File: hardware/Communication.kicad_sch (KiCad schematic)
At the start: 18 parts, among them U1 USBLC6-2SC6, U3 MCP2542FDxMF, U4 USBLC6-2SC6, U6 MCP2542FDxMF

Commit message: symbol update
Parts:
- U3, U6: value MCP2542FDxMF -> MCP2542FD-E/MF; Manufacturer_Part_Number MCP2542FDT-H/MNY -> MCP2542FD-E/MF; Mouser Part Number 579-MCP2542FDT-H/MNY -> 579-MCP2542FD-E/MF; Mouser Price/Stock https://www.mouser.pl/ProductDetail/Microchip-Technology/MCP2542FDT-H-MNY?qs=qdgZG5p0FZ5ii0%252BaLco0zA%3D%3D -> https://www.mouser.pl/ProductDetail/Microchip-Technology/MCP2542FD-E-MF?qs=l7cgNqFNU1jog4BwTzULBw%3D%3D
- renumbered O2 to O5, R40 to R12, R44 to R13, R67 to R15, R45 to R20

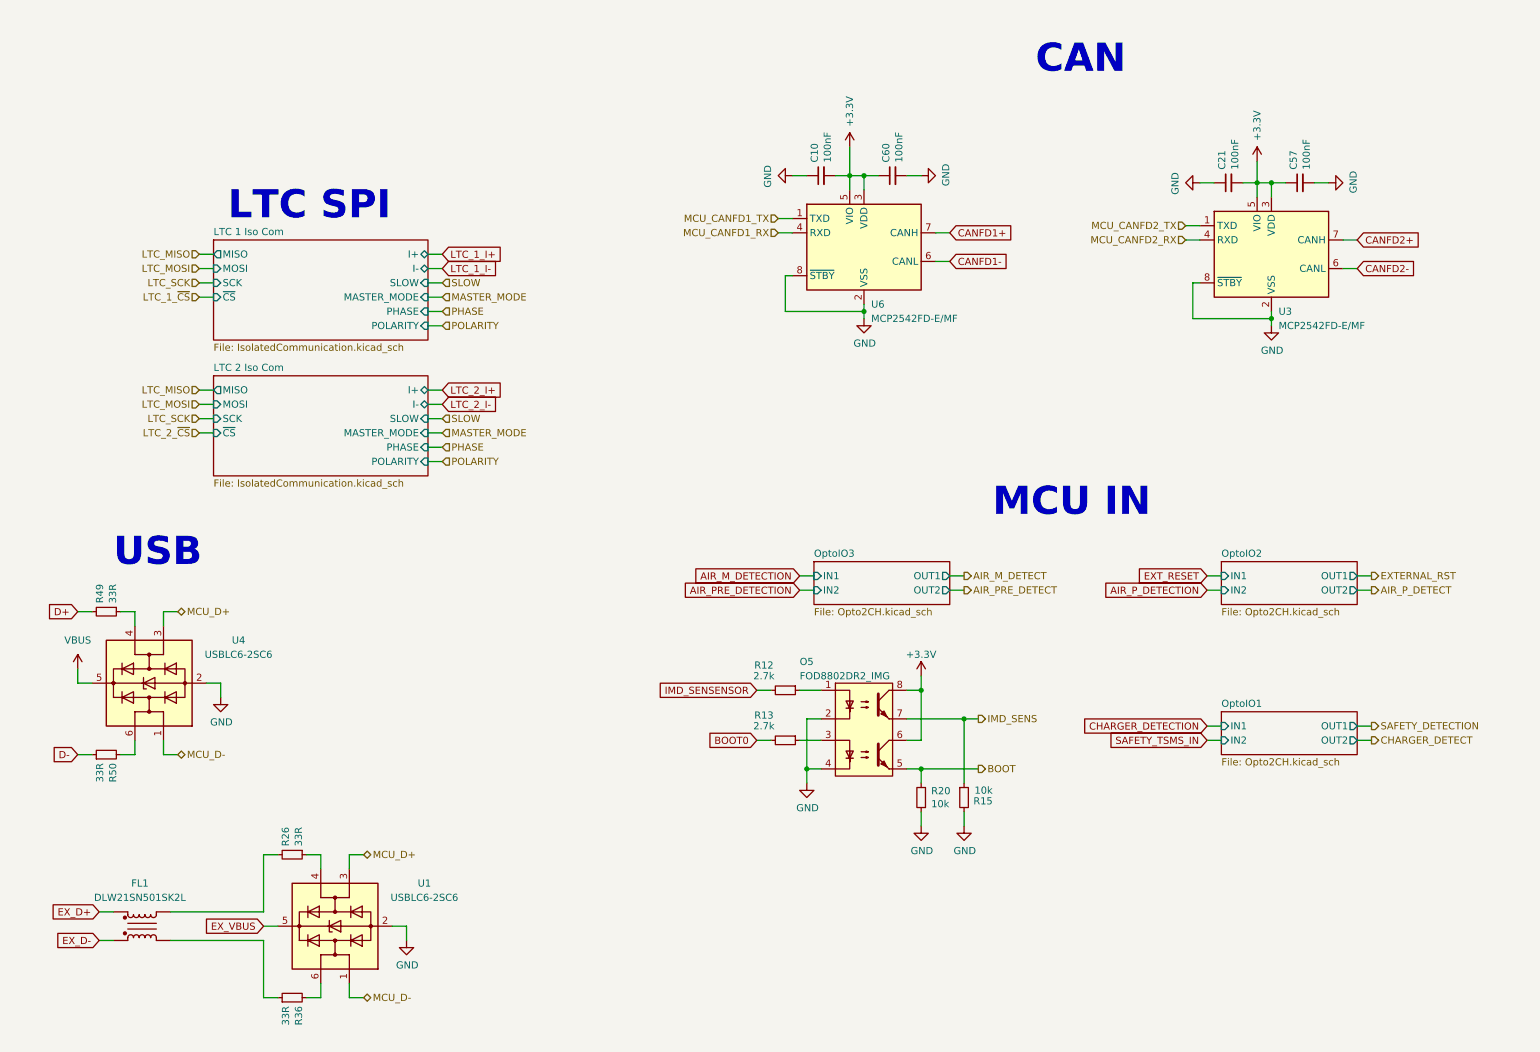
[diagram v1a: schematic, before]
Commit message: schematic clean up
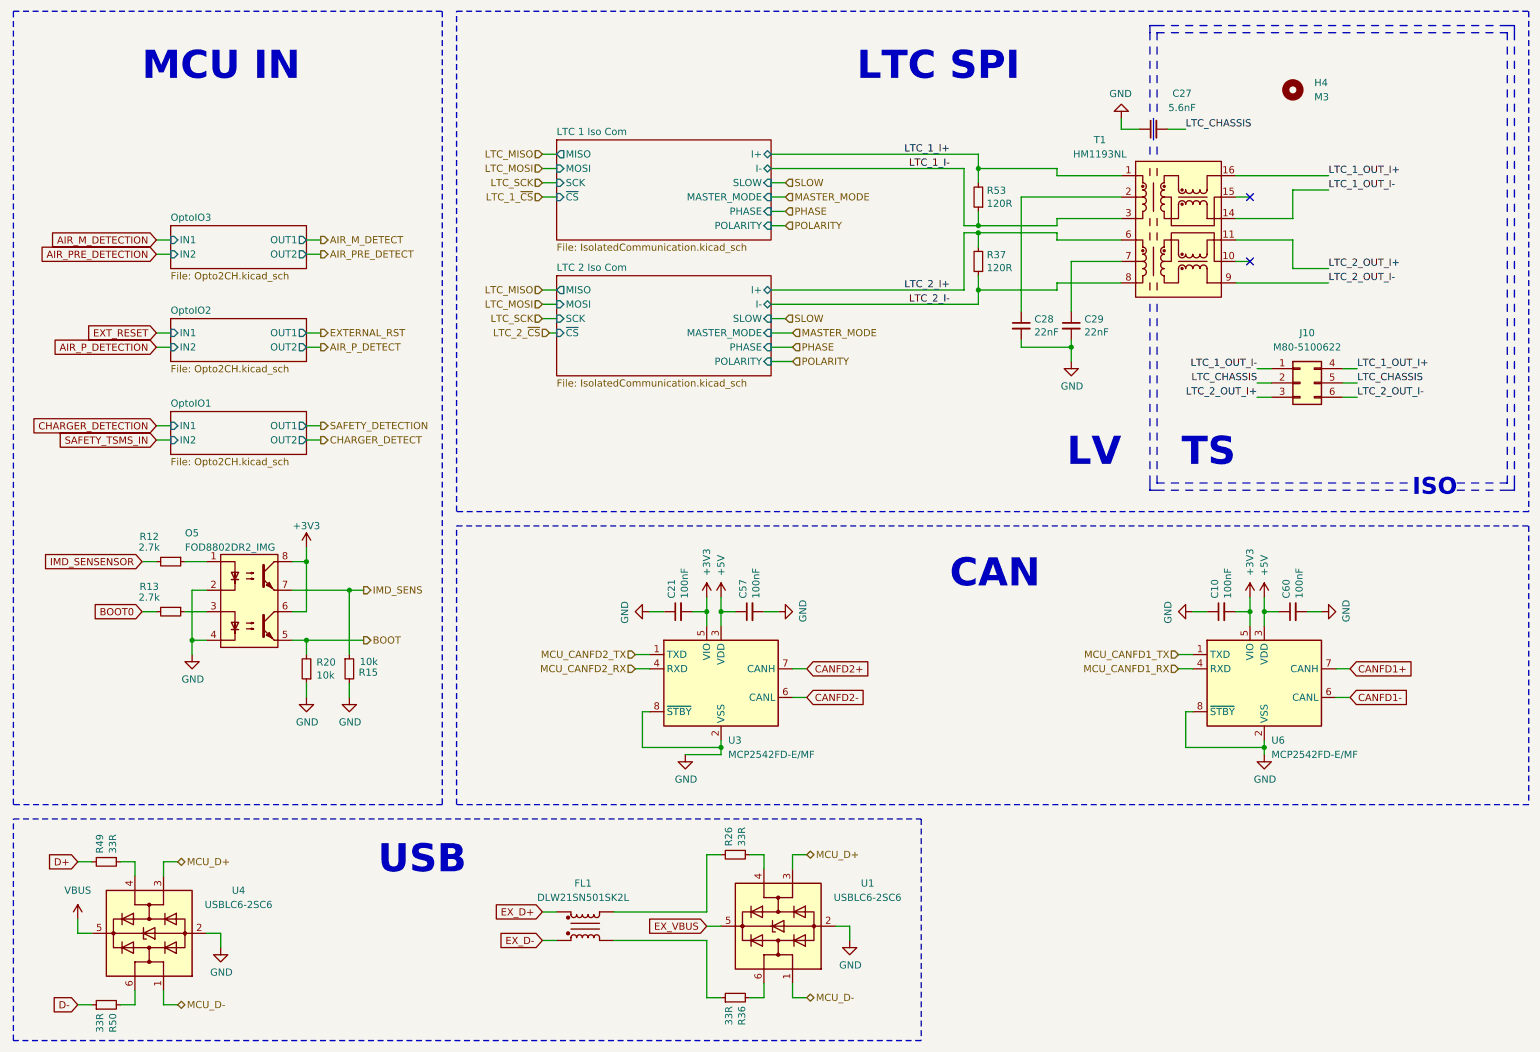
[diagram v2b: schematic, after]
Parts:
- added C27: 5.6nF, Samacsys:C2824, symbol c2824c562jggacauto:C2824C562JGGACAUTO
- added C28, C29: 22nF, Capacitor_SMD:C_0603_1608Metric, symbol Device:C_Small
- added H4: M3, MountingHole:MountingHole_3.2mm_M3, symbol Mechanical:MountingHole
- added J10: M80-5100622, Samacsys:M80-51006YY, symbol Samacsys2:M80-5100622
- added R37, R53: 120R, Resistor_SMD:R_0603_1608Metric, symbol Device:R_Small
- added T1: HM1193NL, Transformer_SMD:Transformer_Pulse_H1100NL, symbol PUTM_EV_BMS_library:HX1188NL
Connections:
- net +3V3: no longer C57.1, C60.1, U3.3 (VDD), U6.3 (VDD)
- net GND: now also C27.1, C28.2, C29.2
- net LTC_1_I+: now also R53.2, T1.1
- net LTC_1_I-: now also R53.1, T1.3
- net LTC_2_I+: now also R37.2, T1.6
- net LTC_2_I-: now also R37.1, T1.8
- new net: C28.1, T1.2
- new net: C29.1, T1.7
- new net +5V: C57.1, C60.1, U3.3 (VDD), U6.3 (VDD)
- new net LTC_1_OUT_I+: J10.4, T1.16
- new net LTC_1_OUT_I-: J10.1, T1.14
- new net LTC_2_OUT_I+: J10.3, T1.11
- new net LTC_2_OUT_I-: J10.6, T1.9
- new net LTC_CHASSIS: C27.2, J10.2, J10.5
- no-connect marks 0 -> 2
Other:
- note added: "ISO"
- note added: "LV"
- note added: "TS"
- moved on the sheet: C10, C21, C57, C60, FL1, O5, R12, R13, R15, R20, R26, R36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

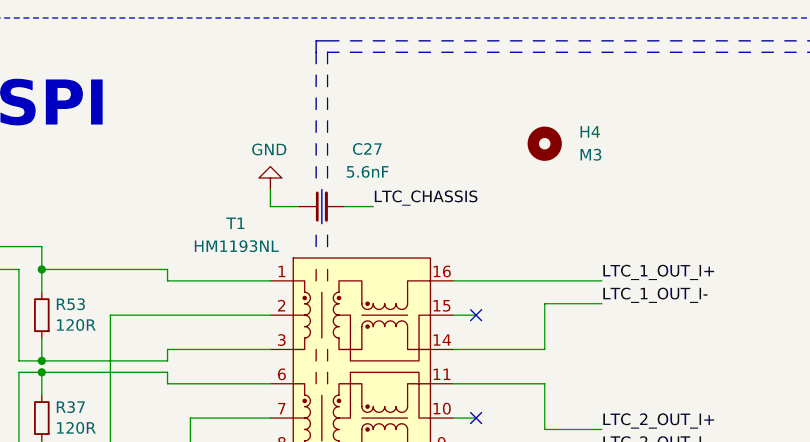
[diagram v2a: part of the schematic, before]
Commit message: relay new driving logic, some ltc communication changes
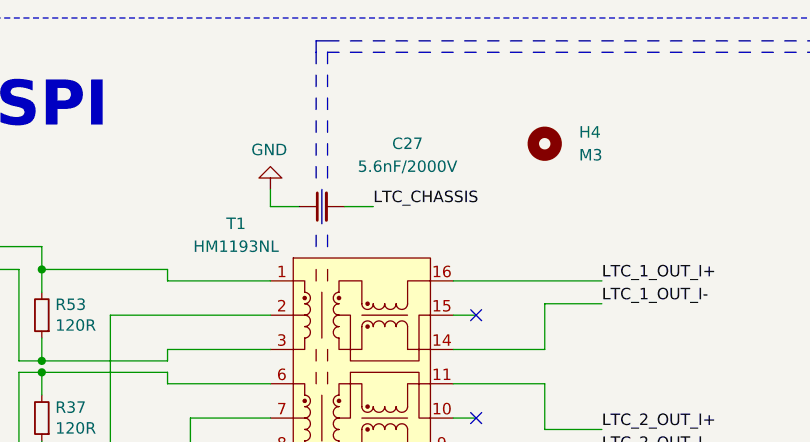
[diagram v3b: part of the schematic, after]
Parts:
- C27: value 5.6nF -> 5.6nF/2000V
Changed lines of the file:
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@@
 		(dnp no)
 		(property "Reference" "C27"
-			(at 221.615 28.575 0)
+			(at 226.06 27.94 0)
 			(effects
 				(font
@@
 			)
 		)
-		(property "Value" "5.6nF"
-			(at 221.615 31.115 0)
+		(property "Value" "5.6nF/2000V"
+			(at 226.06 30.48 0)
 			(effects
 				(font

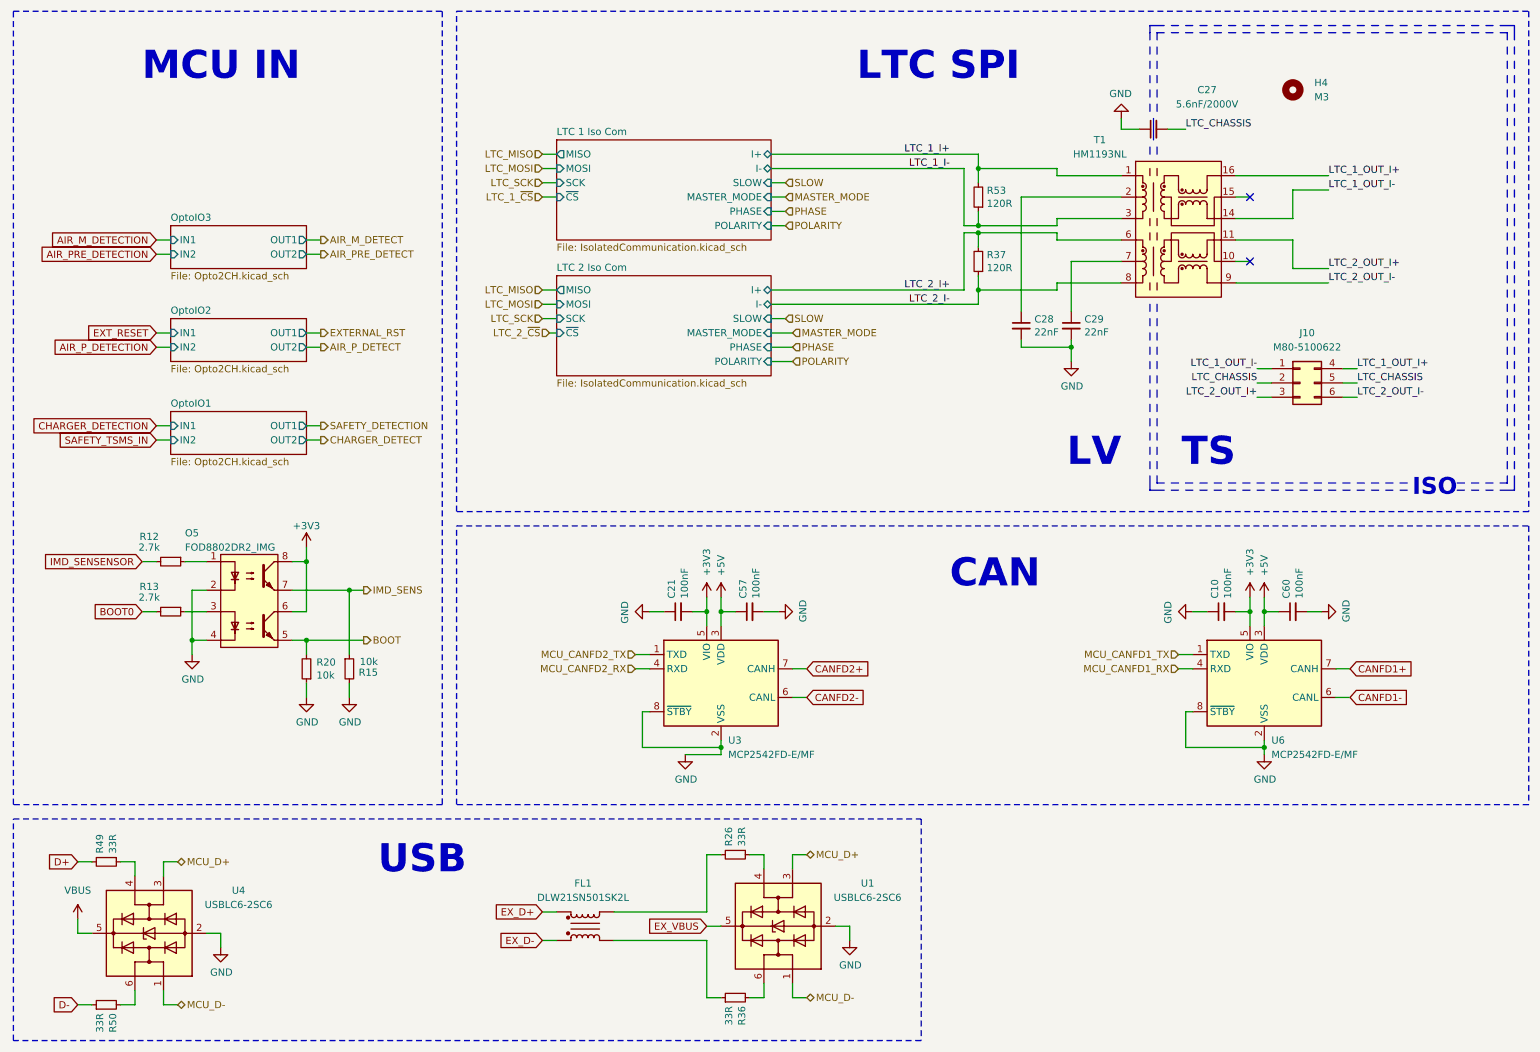
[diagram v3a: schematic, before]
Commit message: relay new driving logic, some ltc communication changes
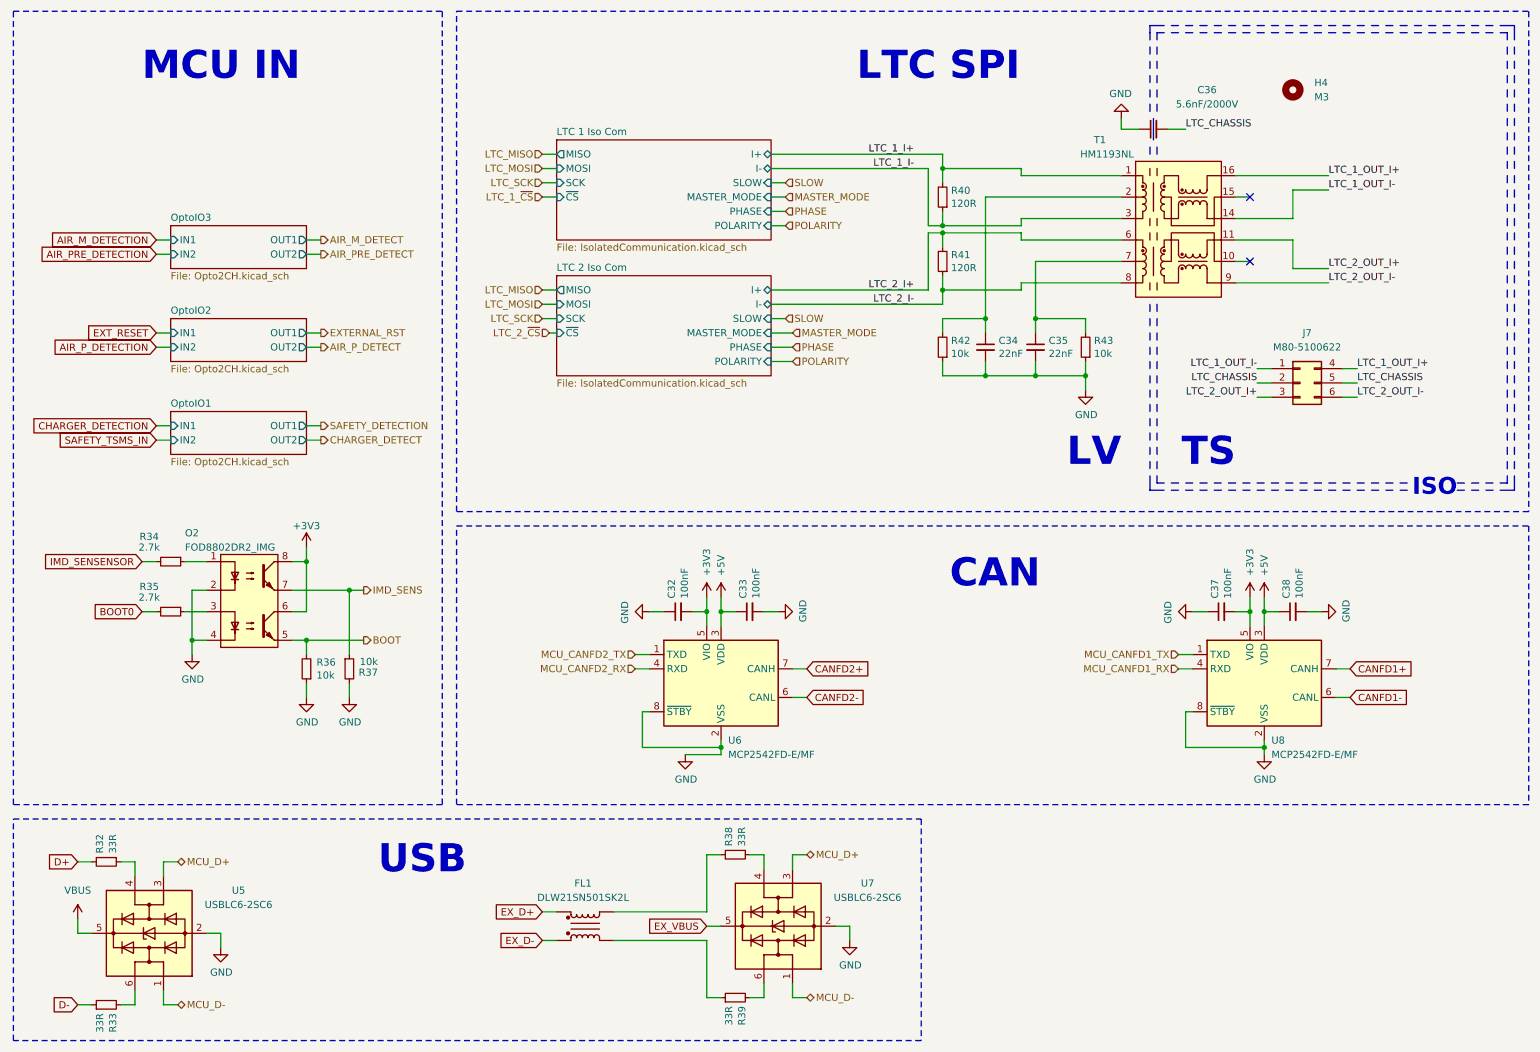
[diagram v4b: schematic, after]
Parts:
- added R42, R43: 10k, Resistor_SMD:R_0603_1608Metric, symbol Device:R_Small
- renumbered C21 to C32, C57 to C33, C28 to C34, C29 to C35, C27 to C36, C10 to C37, C60 to C38, J10 to J7, O5 to O2, R49 to R32, R50 to R33, R12 to R34, R13 to R35, R20 to R36, R15 to R37, R26 to R38, R36 to R39, R53 to R40, R37 to R41, U4 to U5, U3 to U6, U1 to U7, U6 to U8
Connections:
- net GND: now also R42.1, R43.1
- net at C34.1, T1.2: now also R42.2
- net at C35.1, T1.7: now also R43.2
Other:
- moved on the sheet: C34, C35, R40, R41

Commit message: vsv ready
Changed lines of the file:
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@@
 	(hierarchical_label "CHARGER_DETECT"
 		(shape output)
-		(at 68.58 90.17 0)
+		(at 68.58 87.63 0)
 		(fields_autoplaced yes)
 		(effects
@@
 	(hierarchical_label "SAFETY_DETECTION"
 		(shape output)
-		(at 68.58 87.63 0)
+		(at 68.58 90.17 0)
 		(fields_autoplaced yes)
 		(effects

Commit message: major schematic changes
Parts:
- removed H4: M3, MountingHole:MountingHole_3.2mm_M3, symbol Mechanical:MountingHole
- removed O2: FOD8802DR2_IMG, Opto 2 ch:SOIC127P600X175-8N, symbol Opto 2 ch:FOD8802DR2_IMG
- removed R34, R35: 2.7k, Resistor_SMD:R_0603_1608Metric, symbol Device:R_Small
- removed R36, R37: 10k, Resistor_SMD:R_0603_1608Metric, symbol Device:R_Small
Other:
- removed sheet OptoIO1
- removed sheet OptoIO2
- removed sheet OptoIO3
- moved on the sheet: C32, C33, C37, C38, U6, U8
